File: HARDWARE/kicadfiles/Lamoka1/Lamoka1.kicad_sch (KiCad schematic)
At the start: 0 parts

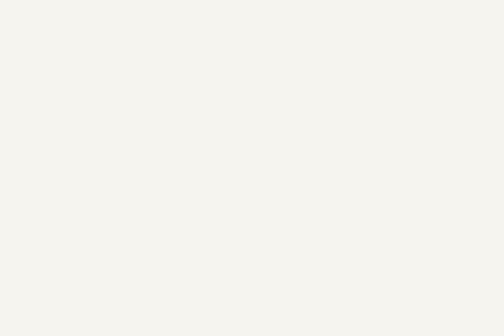
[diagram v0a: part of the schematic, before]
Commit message: Finishing routing for H bridge (Inversion-section)
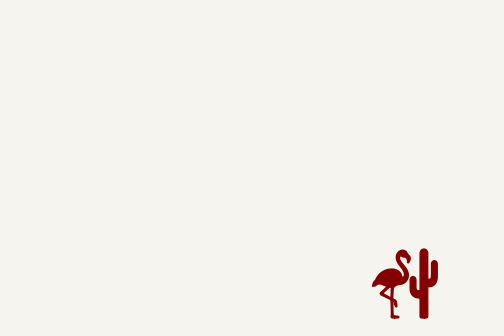
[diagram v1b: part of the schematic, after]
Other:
- company: (none) -> Flamingo & Cactus
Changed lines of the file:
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@@
 	(generator_version "10.0")
 	(paper "A4")
+	(title_block
+		(company "Flamingo & Cactus")
+	)
+	(symbol
+		(lib_id "Flamingo&Cactus-logo:LOGO")
+		(at 181.61 173.99 0)
+		(unit 1)
+		(body_style 1)
+		(exclude_from_sim no)
+		(in_bom yes)
+		(on_board yes)
+		(in_pos_files yes)
+		(dnp no)
+		(fields_autoplaced yes)
+		(property "Reference" "#G1"
+			(at 181.61 169.6241 0)
+			(hide yes)
+			(show_name no)
+			(do_not_autoplace no)
+			(effects
+				(font
+					(size 1.27 1.27)
+				)
+			)
+		)
+		(property "Value" "LOGO"
+			(at 181.61 178.3559 0)
+			(hide yes)
+			(show_name no)
+			(do_not_autoplace no)
+			(effects
+				(font
+					(size 1.27 1.27)
+				)
+			)
+		)
+		(property "Footprint" "Package_LCC:PLCC-84_29.3x29.3mm_P1.27mm"
+			(at 181.61 173.99 0)
+			(hide yes)
+			(show_name no)
+			(do_not_autoplace no)
+			(effects
+				(font
+					(size 1.27 1.27)
+				)
+			)
+		)
+		(property "Datasheet" ""
+			(at 181.61 173.99 0)
+			(hide yes)
+			(show_name no)
+			(do_not_autoplace no)
+			(effects
+				(font
+					(size 1.27 1.27)
+				)
+			)
+		)
+		(property "Description" ""
+			(at 181.61 173.99 0)
+			(hide yes)
+			(show_name no)
+			(do_not_autoplace no)
+			(effects
+				(font
+					(size 1.27 1.27)
+				)
+			)
+		)
+		(instances
+			(project "Lamoka1"
+				(path "/c7bb62b6-932f-49c1-a356-0286e905fc0a"
+					(reference "#G1")
+					(unit 1)
+				)
+			)
+		)
+	)
 	(sheet
 		(at 108.966 22.86)

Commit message: ADD logo, repo grade, and cosmetic/finishing H bridge connections
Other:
- sheet Control-section ports: added GPIO1, GPIO2, GPIO3, GPIO4; removed none
- sheet Inversion-section ports: added GPIO1, GPIO2, GPIO3, GPIO4; removed none
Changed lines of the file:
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@@
 		(company "Flamingo & Cactus")
+	)
+	(wire
+		(pts
+			(xy 99.06 45.72) (xy 109.22 45.72)
+		)
+		(stroke
+			(width 0)
+			(type default)
+		)
+	)
+	(wire
+		(pts
+			(xy 99.06 53.34) (xy 109.22 53.34)
+		)
+		(stroke
+			(width 0)
+			(type default)
+		)
+	)
+	(wire
+		(pts
+			(xy 99.06 41.91) (xy 109.22 41.91)
+		)
+		(stroke
+			(width 0)
+			(type default)
+		)
+	)
+	(wire
+		(pts
+			(xy 99.06 49.53) (xy 109.22 49.53)
+		)
+		(stroke
+			(width 0)
+			(type default)
+		)
 	)
 	(symbol
@@
 	)
 	(sheet
-		(at 108.966 22.86)
+		(at 109.22 22.86)
 		(size 81.534 52.07)
 		(exclude_from_sim no)
@@
 		)
 		(property "Sheetname" "Inversion-section"
-			(at 108.966 22.1484 0)
+			(at 109.22 22.1484 0)
 			(show_name no)
 			(do_not_autoplace no)
@@
 		)
 		(property "Sheetfile" "Inversion-section.kicad_sch"
-			(at 108.966 75.5146 0)
+			(at 109.22 75.5146 0)
 			(show_name no)
 			(do_not_autoplace no)
@@
 		)
 		(pin "11-14v input" input
-			(at 108.966 34.29 180)
+			(at 109.22 34.29 180)
+			(effects
+				(font
+					(size 1.27 1.27)
+				)
+				(justify left)
+			)
+		)
+		(pin "GPIO4" input
+			(at 109.22 41.91 180)
+			(effects
+				(font
+					(size 1.27 1.27)
+				)
+				(justify left)
+			)
+		)
+		(pin "GPIO3" input
+			(at 109.22 45.72 180)
+			(effects
+				(font
+					(size 1.27 1.27)
+				)
+				(justify left)
+			)
+		)
+		(pin "GPIO2" input
+			(at 109.22 49.53 180)
+			(effects
+				(font
+					(size 1.27 1.27)
+				)
+				(justify left)
+			)
+		)
+		(pin "GPIO1" input
+			(at 109.22 53.34 180)
 			(effects
 				(font
@@
 			)
 		)
+		(pin "GPIO4" input
+			(at 99.06 41.91 0)
+			(effects
+				(font
+					(size 1.27 1.27)
+				)
+				(justify right)
+			)
+		)
+		(pin "GPIO3" input
+			(at 99.06 45.72 0)
+			(effects
+				(font
+					(size 1.27 1.27)
+				)
+				(justify right)
+			)
+		)
+		(pin "GPIO2" input
+			(at 99.06 49.53 0)
+			(effects
+				(font
+					(size 1.27 1.27)
+				)
+				(justify right)
+			)
+		)
+		(pin "GPIO1" input
+			(at 99.06 53.34 0)
+			(effects
+				(font
+					(size 1.27 1.27)
+				)
+				(justify right)
+			)
+		)

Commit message: Improving repository
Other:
- sheet Control-section renamed Control-Section
- sheet Inversion-section renamed Inversion-Section
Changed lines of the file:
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@@
 	(generator "eeschema")
 	(generator_version "10.0")
-	(paper "A4")
+	(paper "A5")
 	(title_block
 		(company "Flamingo & Cactus")
@@
 	(symbol
 		(lib_id "Flamingo&Cactus-logo:LOGO")
-		(at 181.61 173.99 0)
+		(at 95.25 111.76 0)
 		(unit 1)
 		(body_style 1)
@@
 		(fields_autoplaced yes)
 		(property "Reference" "#G1"
-			(at 181.61 169.6241 0)
+			(at 95.25 107.3941 0)
 			(hide yes)
 			(show_name no)
@@
 		)
 		(property "Value" "LOGO"
-			(at 181.61 178.3559 0)
+			(at 95.25 116.1259 0)
 			(hide yes)
 			(show_name no)
@@
 		)
 		(property "Footprint" "Package_LCC:PLCC-84_29.3x29.3mm_P1.27mm"
-			(at 181.61 173.99 0)
+			(at 95.25 111.76 0)
 			(hide yes)
 			(show_name no)
@@
 		)
 		(property "Datasheet" ""
-			(at 181.61 173.99 0)
+			(at 95.25 111.76 0)
 			(hide yes)
 			(show_name no)
@@
 		)
 		(property "Description" ""
-			(at 181.61 173.99 0)
+			(at 95.25 111.76 0)
 			(hide yes)
 			(show_name no)
@@
 			(color 0 0 0 0)
 		)
-		(property "Sheetname" "Inversion-section"
+		(property "Sheetname" "Inversion-Section"
 			(at 109.22 22.1484 0)
 			(show_name no)
@@
 			(color 0 0 0 0)
 		)
-		(property "Sheetname" "Control-section"
+		(property "Sheetname" "Control-Section"
 			(at 24.13 22.4024 0)
 			(show_name no)

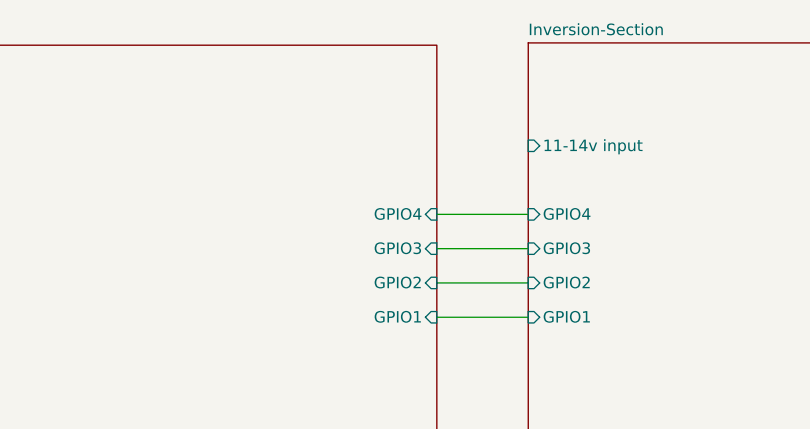
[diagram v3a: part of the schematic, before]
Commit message: ADD fan connection, and finish buck converter 5v
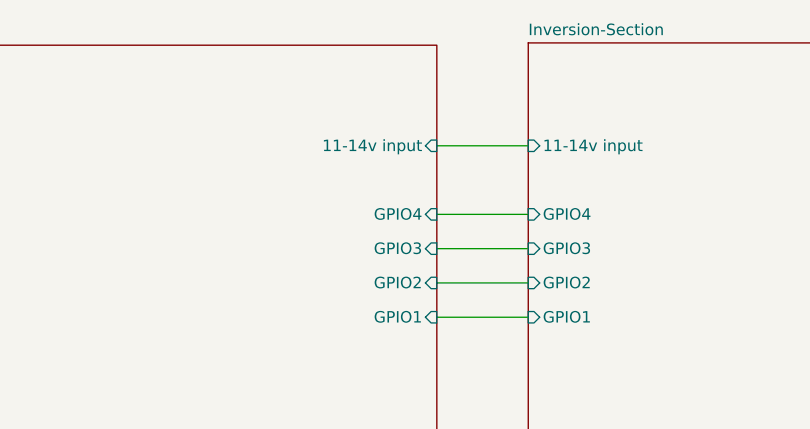
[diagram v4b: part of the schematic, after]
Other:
- sheet Control-Section ports: added 11-14v input; removed none
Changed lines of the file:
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@@
+		)
+	)
+	(wire
+		(pts
+			(xy 99.06 34.29) (xy 109.22 34.29)
+		)
+		(stroke
+			(width 0)
+			(type default)
 		)
 	)
@@
 			(effects
 				(font
+					(size 1.27 1.27)
+				)
+				(justify right)
+			)
+		)
+		(pin "11-14v input" input
+			(at 99.06 34.29 0)
+			(effects
+				(font

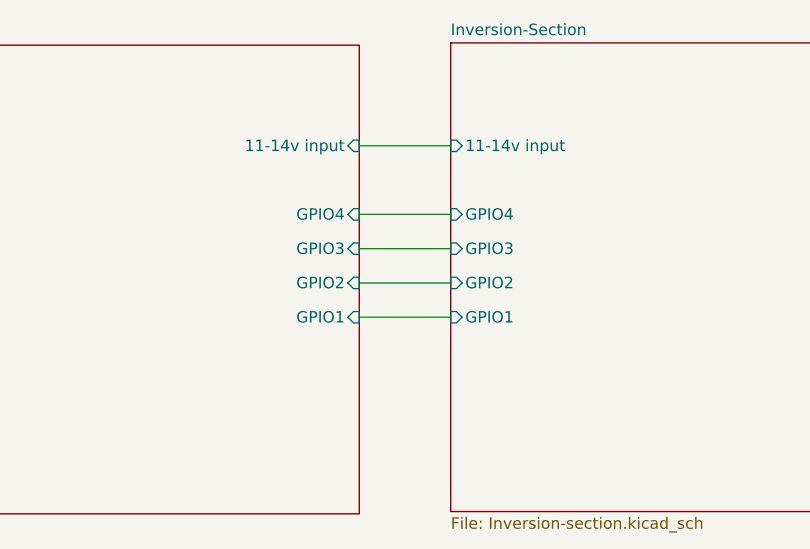
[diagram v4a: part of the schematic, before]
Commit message: ADD temp sensors, more doccumentation regarding design
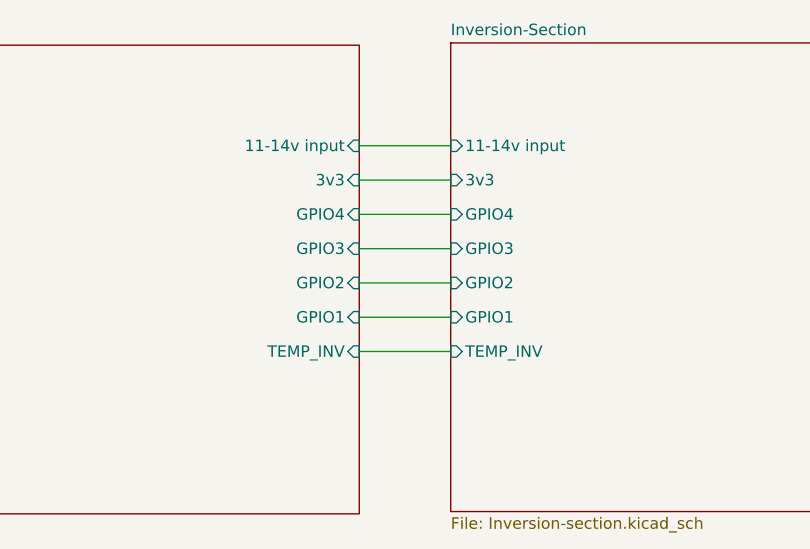
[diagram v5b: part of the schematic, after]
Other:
- sheet Control-Section ports: added 3v3, TEMP_INV; removed none
- sheet Inversion-Section ports: added 3v3, TEMP_INV; removed none
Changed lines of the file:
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@@
+	(wire
+		(pts
+			(xy 99.06 57.15) (xy 109.22 57.15)
+		)
+		(stroke
+			(width 0)
+			(type default)
+		)
+	)
 	(wire
 		(pts
@@
 		(pts
 			(xy 99.06 49.53) (xy 109.22 49.53)
+		)
+		(stroke
+			(width 0)
+			(type default)
+		)
+	)
+	(wire
+		(pts
+			(xy 99.06 38.1) (xy 109.22 38.1)
 		)
 		(stroke
@@
 			)
 		)
+		(pin "3v3" input
+			(at 109.22 38.1 180)
+			(effects
+				(font
+					(size 1.27 1.27)
+				)
+				(justify left)
+			)
+		)
+		(pin "TEMP_INV" input
+			(at 109.22 57.15 180)
+			(effects
+				(font
+					(size 1.27 1.27)
+				)
+				(justify left)
+			)
+		)
 		(instances
 			(project "Lamoka1"
@@
 			(effects
 				(font
+					(size 1.27 1.27)
+				)
+				(justify right)
+			)
+		)
+		(pin "3v3" input
+			(at 99.06 38.1 0)
+			(effects
+				(font
+					(size 1.27 1.27)
+				)
+				(justify right)
+			)
+		)
+		(pin "TEMP_INV" input
+			(at 99.06 57.15 0)
+			(effects
+				(font

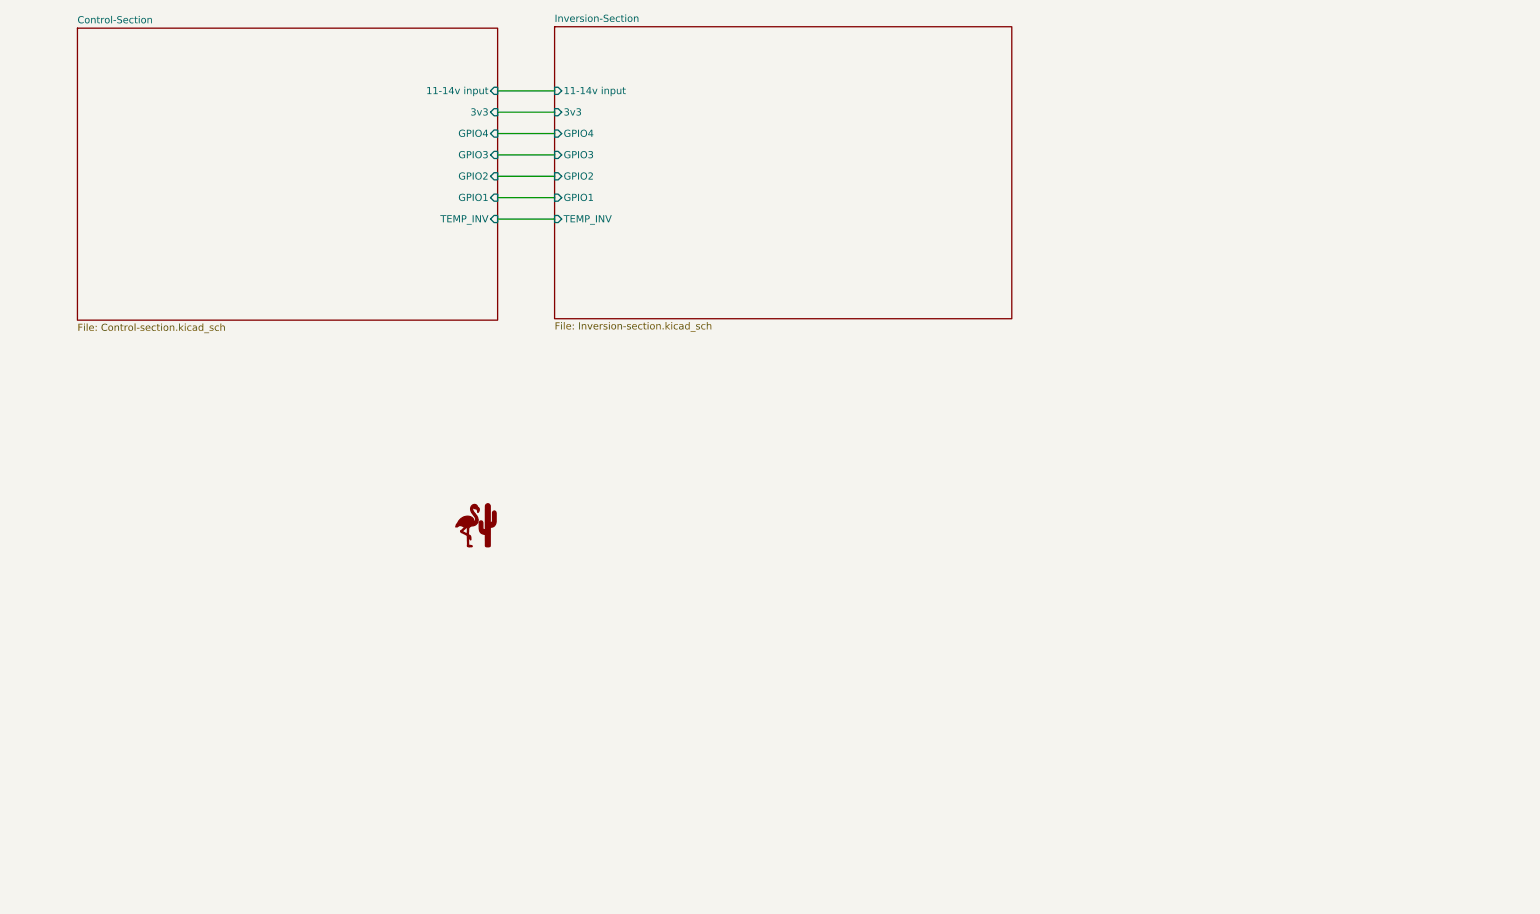
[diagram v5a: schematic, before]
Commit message: ADD better format for connectors, output connector, transformer connector, and more
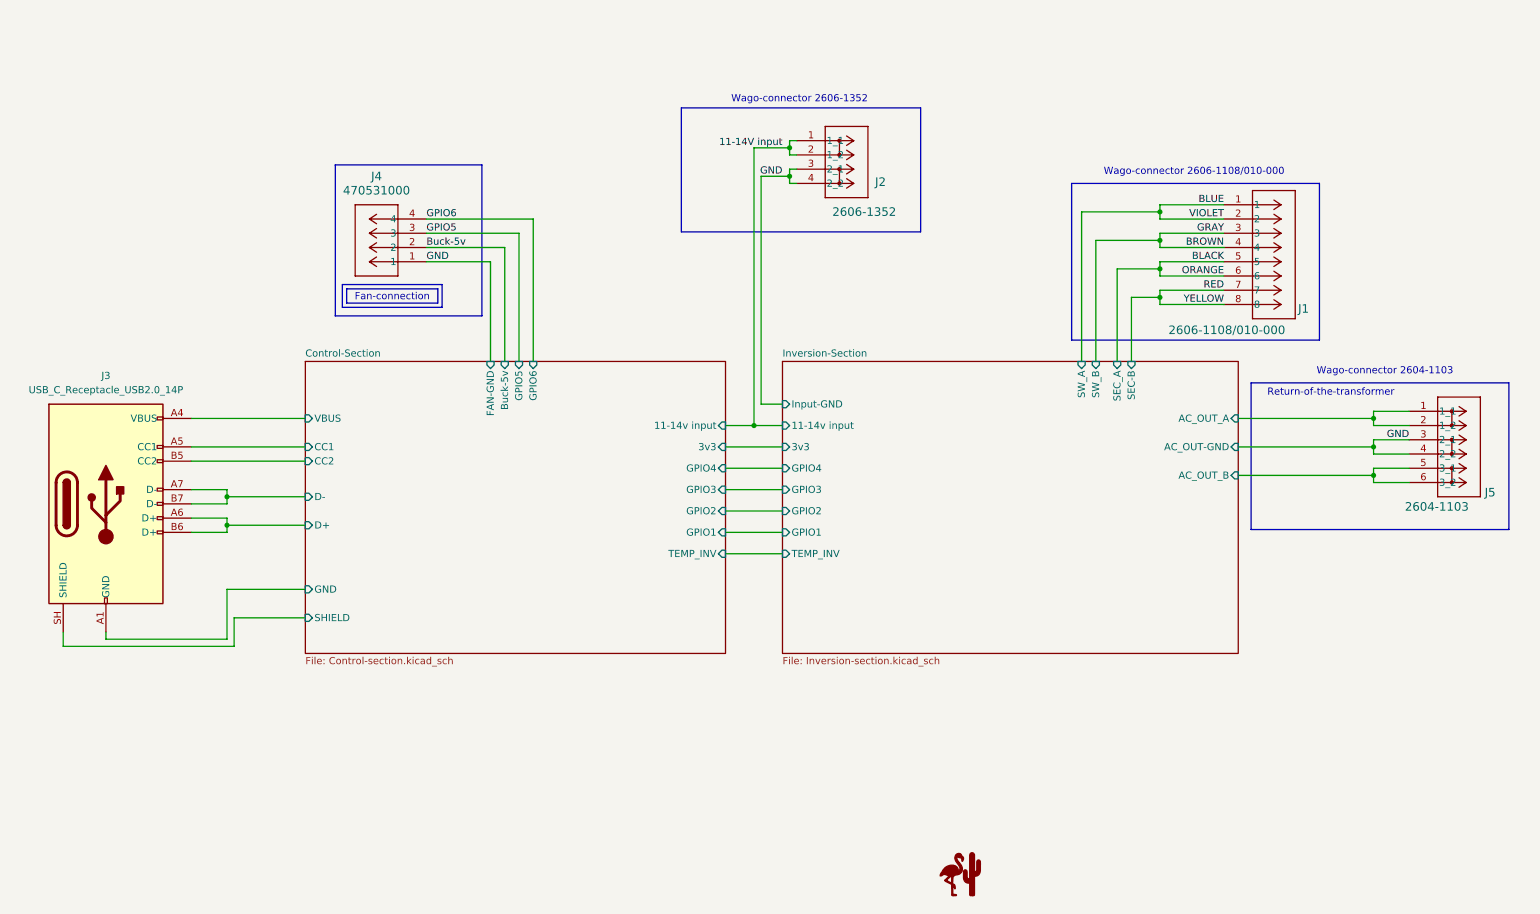
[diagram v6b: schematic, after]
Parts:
- added J1: 2606-1108/010-000, CONN8_2606-1108/010-000_WAG, symbol 2606-1108/010-000:2606-1108_010-000
- added J2: 2606-1352, CONN2_2606-1352_WAG, symbol Wago-connector:2606-1352
- added J3: USB_C_Receptacle_USB2.0_14P, Connector_USB:USB_C_Receptacle_HRO_TYPE-C-31-M-12, symbol Connector:USB_C_Receptacle_USB2.0_14P
- added J4: 470531000, CONN_SD-47053-001_H10p00_MOL, symbol 470531000:470531000
- added J5: 2604-1103, CONN3_2604-1103_WAG, symbol 2604-1103:2604-1103
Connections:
- new net 11-14V input: J2.1 (1_1), J2.2 (1_2)
- new net BLACK: J1.5, J1.6
- new net BLUE: J1.1, J1.2
- new net BROWN: J1.3, J1.4
- new net Buck-5v: J4.2
- new net Control-Section/CC1: J3.A5 (CC1)
- new net Control-Section/CC2: J3.B5 (CC2)
- new net Control-Section/D+: J3.A6 (D+), J3.B6 (D+)
- new net Control-Section/D-: J3.A7 (D-), J3.B7 (D-)
- new net Control-Section/GND: J3.A1 (GND), J3.A12 (GND), J3.B1 (GND), J3.B12 (GND)
- new net Control-Section/SHIELD: J3.SH (SHIELD)
- new net Control-Section/VBUS: J3.A4 (VBUS), J3.A9 (VBUS), J3.B4 (VBUS), J3.B9 (VBUS)
- new net GND: J2.3 (2_1), J2.4 (2_2), J4.1, J5.3 (2_1), J5.4 (2_2)
- new net GPIO5: J4.3
- new net GPIO6: J4.4
- new net Inversion-Section/AC_OUT_A: J5.1 (1_1), J5.2 (1_2)
- new net Inversion-Section/AC_OUT_B: J5.5 (3_1), J5.6 (3_2)
- new net RED: J1.7, J1.8
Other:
- sheet Control-Section ports: added Buck-5v, CC1, CC2, D+, D-, FAN-GND, GND, GPIO5, GPIO6, SHIELD, VBUS; removed none
- sheet Inversion-Section ports: added AC_OUT-GND, AC_OUT_A, AC_OUT_B, Input-GND, SEC-B, SEC_A, SW_A, SW_B; removed none
- note added: "Fan-connection"
- note added: "Return-of-the-transformer"
- note added: "Wago-connector 2604-1103"
- note added: "Wago-connector 2606-1108/010-000"
- note added: "Wago-connector 2606-1352"
